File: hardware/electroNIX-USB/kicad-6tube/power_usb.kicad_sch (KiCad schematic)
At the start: 13 parts, among them J1 USB-C (USB 2.0), U1 USBLC6-2SC6, U2 AMS1117-3.3, U3 CH340C

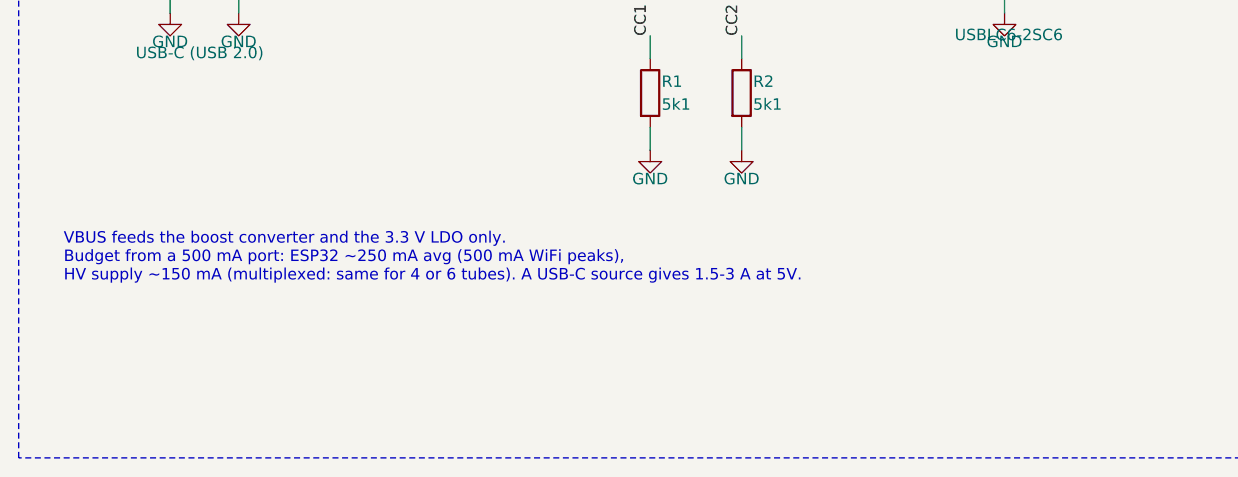
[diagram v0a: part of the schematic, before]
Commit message: electroNIX-USB: apply RFT Z573M data sheet, add tube footprint
The data book confirms the pinout already in the symbol. The tube is
side-view (not top-view), with 13 flying leads on a 9.53 mm circle and
wire 7 at the front. New footprint electronix:Nixie_RFT_Z573M (top
view, wire 7 toward the front edge) is assigned to the tubes.

Tube current: Ik is 1.5-2.5 mA continuous, 12 mA pulse. PCB-036's 10k
anode resistors averaged only ~0.75 mA per tube when multiplexed. Anode
resistors are now 5k6 (4 tubes) and 3k9 (6 tubes), cathode base
resistors 6k8. To carry the extra HV power, the ladder caps go to
2.2 uF and the 6-tube build uses a 22 uH inductor.

Co-Authored-By: Claude Opus 5.5 <noreply@anthropic.com>
Claude-Session: https://claude.ai/code/session_01AFMfevKEKDGbci8uJGhf4W
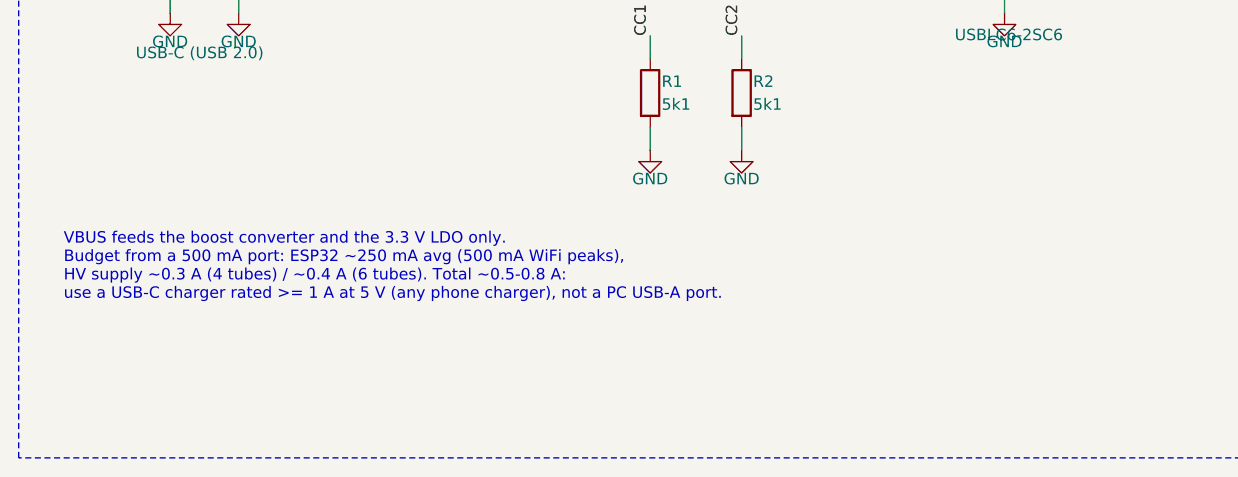
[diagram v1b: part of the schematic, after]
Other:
- note added: "VBUS feeds the boost converter and the 3.3 V LDO only. Budget from a 500 mA port: ESP32 ~250 mA avg (500 mA WiFi peaks), HV supply ~0.3 A (4 tubes) / ~0.4 A (6 tubes). Total ~0.5-0.8 A: use a USB-C charger rated >= 1 A at 5 V (any phone charger), not a PC USB-A port."
- note removed: "VBUS feeds the boost converter and the 3.3 V LDO only. Budget from a 500 mA port: ESP32 ~250 mA avg (500 mA WiFi peaks), HV supply ~150 mA (multiplexed: same for 4 or 6 tubes). A USB-C source gives 1.5-3 A at 5V."
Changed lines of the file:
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@@
       (justify left top))
 )
-  (text "VBUS feeds the boost converter and the 3.3 V LDO only.\nBudget from a 500 mA port: ESP32 ~250 mA avg (500 mA WiFi peaks),\nHV supply ~150 mA (multiplexed: same for 4 or 6 tubes). A USB-C source gives 1.5-3 A at 5V."
+  (text "VBUS feeds the boost converter and the 3.3 V LDO only.\nBudget from a 500 mA port: ESP32 ~250 mA avg (500 mA WiFi peaks),\nHV supply ~0.3 A (4 tubes) / ~0.4 A (6 tubes). Total ~0.5-0.8 A:\nuse a USB-C charger rated >= 1 A at 5 V (any phone charger), not a PC USB-A port."
     (at 25 140 0)
     (effects

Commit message: electroNIX-USB: tantalum bulk caps on the 5 V input and boost input
Back to PCB-036's 22 uF/35 V tantalum (7343 D case) for the boost input
and use the same part for the USB-C bulk cap. It holds its value at 5 V,
unlike a small MLCC, and its ESR damps hot-plug ringing on the cable.
The 100 nF ceramics stay. Placement adjusted around the larger parts.

Co-Authored-By: Claude Opus 5.5 <noreply@anthropic.com>
Claude-Session: https://claude.ai/code/session_01AFMfevKEKDGbci8uJGhf4W
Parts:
- C1: value 22u 10V -> 22u 35V tant.; footprint Capacitor_SMD:C_1206_3216Metric -> Capacitor_Tantalum_SMD:CP_EIA-7343-31_Kemet-D; symbol Device:C -> Device:C_Polarized
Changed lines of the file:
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@@
           (unit 1)))))
   (symbol
-    (lib_id "Device:C")
+    (lib_id "Device:C_Polarized")
     (at 154.94 59.69 0)
     (unit 1)
@@
           (size 1.27 1.27))
         (justify left)))
-    (property "Value" "22u 10V"
+    (property "Value" "22u 35V tant."
       (at 156.21 60.96 0)
       (effects
@@
           (size 1.27 1.27))
         (justify left)))
-    (property "Footprint" "Capacitor_SMD:C_1206_3216Metric"
+    (property "Footprint" "Capacitor_Tantalum_SMD:CP_EIA-7343-31_Kemet-D"
       (at 154.94 59.69 0)
       (effects
